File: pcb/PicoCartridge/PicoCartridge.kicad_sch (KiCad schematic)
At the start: 0 parts

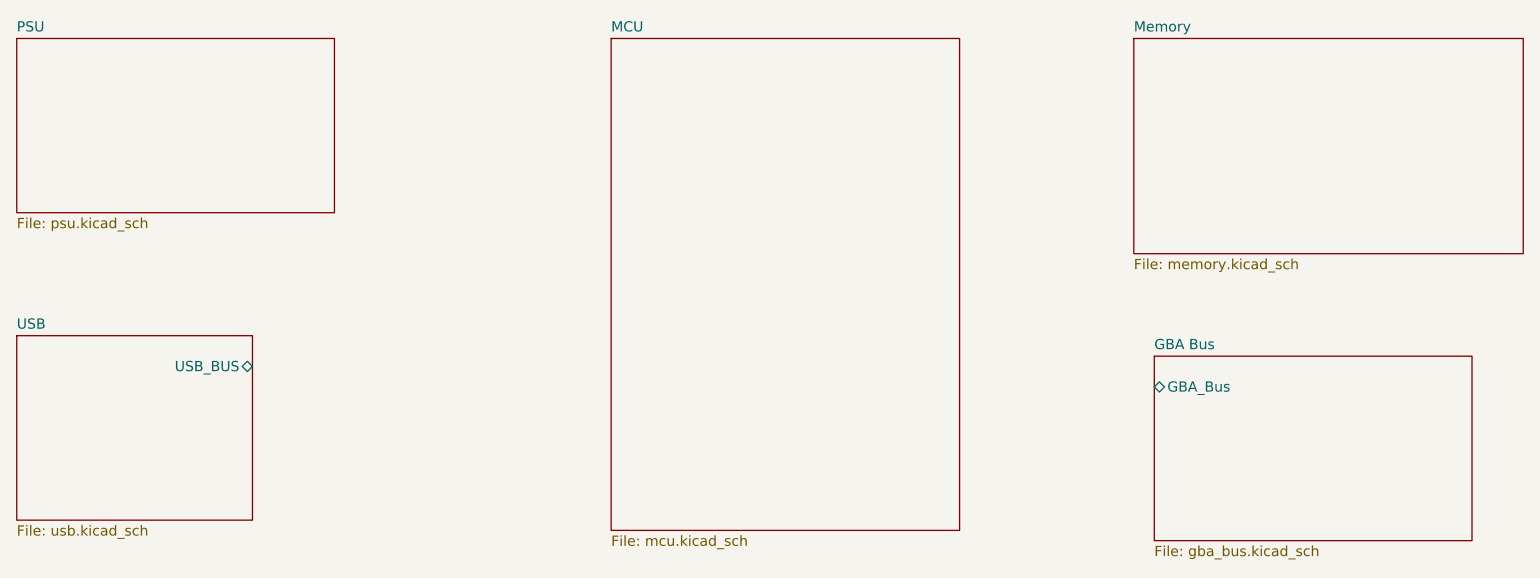
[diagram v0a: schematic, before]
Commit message: Defined additional interfaces
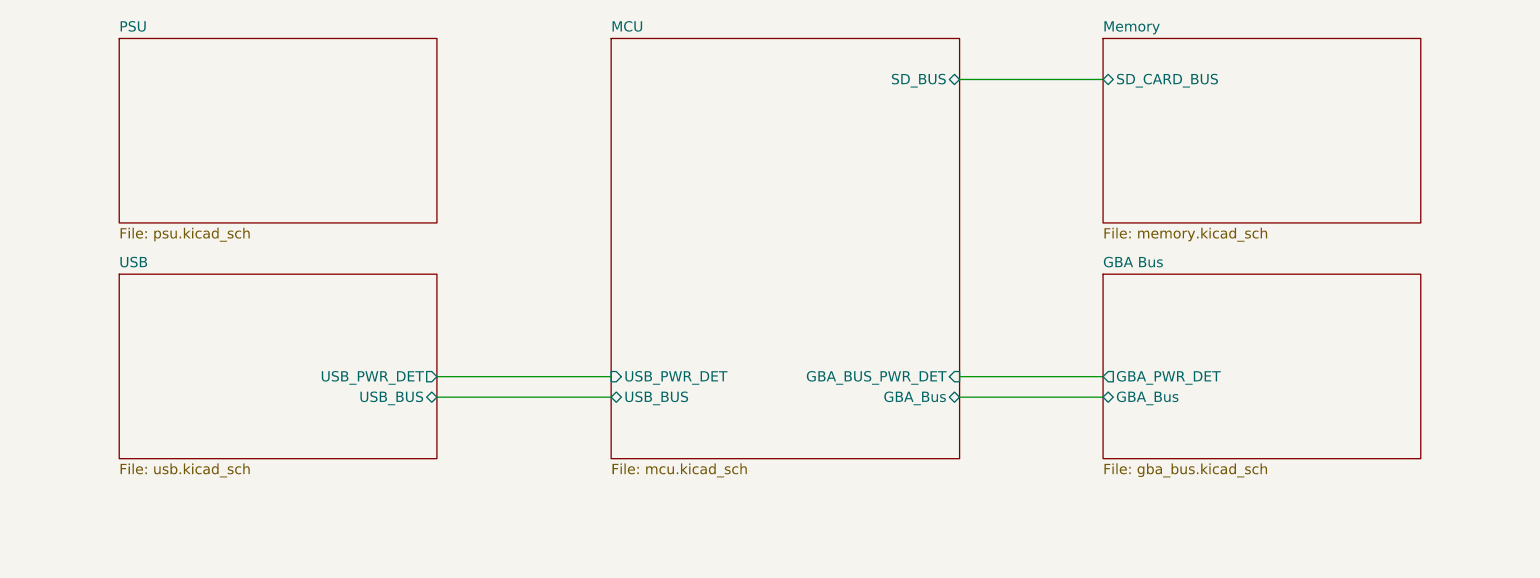
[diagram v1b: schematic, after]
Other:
- sheet GBA Bus ports: added GBA_PWR_DET; removed none
- sheet MCU ports: added GBA_BUS_PWR_DET, GBA_Bus, SD_BUS, USB_BUS, USB_PWR_DET; removed none
- sheet Memory ports: added SD_CARD_BUS; removed none
- sheet USB ports: added USB_PWR_DET; removed none
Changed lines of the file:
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@@
 	(generator_version "8.0")
 	(paper "A4")
-	(sheet
-		(at 21.59 25.4)
-		(size 39.37 21.59)
+	(wire
+		(pts
+			(xy 138.43 30.48) (xy 156.21 30.48)
+		)
+		(stroke
+			(width 0)
+			(type default)
+		)
+	)
+	(wire
+		(pts
+			(xy 138.43 69.85) (xy 156.21 69.85)
+		)
+		(stroke
+			(width 0)
+			(type default)
+		)
+	)
+	(wire
+		(pts
+			(xy 73.66 69.85) (xy 95.25 69.85)
+		)
+		(stroke
+			(width 0)
+			(type default)
+		)
+	)
+	(wire
+		(pts
+			(xy 73.66 67.31) (xy 95.25 67.31)
+		)
+		(stroke
+			(width 0)
+			(type default)
+		)
+	)
+	(wire
+		(pts
+			(xy 138.43 67.31) (xy 156.21 67.31)
+		)
+		(stroke
+			(width 0)
+			(type default)
+		)
+	)
+	(sheet
+		(at 34.29 25.4)
+		(size 39.37 22.86)
 		(fields_autoplaced yes)
 		(stroke
@@
 		)
 		(property "Sheetname" "PSU"
-			(at 21.59 24.6884 0)
+			(at 34.29 24.6884 0)
 			(effects
 				(font
@@
 		)
 		(property "Sheetfile" "psu.kicad_sch"
-			(at 21.59 47.5746 0)
+			(at 34.29 48.8446 0)
 			(effects
 				(font
@@
 	)
 	(sheet
-		(at 162.56 64.77)
+		(at 156.21 54.61)
 		(size 39.37 22.86)
 		(fields_autoplaced yes)
@@
 		)
 		(property "Sheetname" "GBA Bus"
-			(at 162.56 64.0584 0)
+			(at 156.21 53.8984 0)
 			(effects
 				(font
@@
 		)
 		(property "Sheetfile" "gba_bus.kicad_sch"
-			(at 162.56 88.2146 0)
+			(at 156.21 78.0546 0)
 			(effects
 				(font
@@
 		)
 		(pin "GBA_Bus" bidirectional
-			(at 162.56 68.58 180)
+			(at 156.21 69.85 180)
+			(effects
+				(font
+					(size 1.27 1.27)
+				)
+				(justify left)
+			)
+		)
+		(pin "GBA_PWR_DET" output
+			(at 156.21 67.31 180)
 			(effects
 				(font
@@
 	)
 	(sheet
-		(at 21.59 62.23)
-		(size 29.21 22.86)
+		(at 34.29 54.61)
+		(size 39.37 22.86)
 		(fields_autoplaced yes)
 		(stroke
@@
 		)
 		(property "Sheetname" "USB"
-			(at 21.59 61.5184 0)
+			(at 34.29 53.8984 0)
 			(effects
 				(font
@@
 		)
 		(property "Sheetfile" "usb.kicad_sch"
-			(at 21.59 85.6746 0)
+			(at 34.29 78.0546 0)
 			(effects
 				(font
@@
 		)
 		(pin "USB_BUS" bidirectional
-			(at 50.8 66.04 0)
+			(at 73.66 69.85 0)
+			(effects
+				(font
+					(size 1.27 1.27)
+				)
+				(justify right)
+			)
+		)
+		(pin "USB_PWR_DET" output
+			(at 73.66 67.31 0)
 			(effects
 				(font
@@
 	)
 	(sheet
-		(at 160.02 25.4)
-		(size 48.26 26.67)
+		(at 156.21 25.4)
+		(size 39.37 22.86)
 		(fields_autoplaced yes)
 		(stroke
@@
 		)
 		(property "Sheetname" "Memory"
-			(at 160.02 24.6884 0)
+			(at 156.21 24.6884 0)
 			(effects
 				(font
@@
 		)
 		(property "Sheetfile" "memory.kicad_sch"
-			(at 160.02 52.6546 0)
-			(effects
-				(font
-					(size 1.27 1.27)
-				)
-				(justify left top)
+			(at 156.21 48.8446 0)
+			(effects
+				(font
+					(size 1.27 1.27)
+				)
+				(justify left top)
+			)
+		)
+		(pin "SD_CARD_BUS" bidirectional
+			(at 156.21 30.48 180)
+			(effects
+				(font
+					(size 1.27 1.27)
+				)
+				(justify left)
 			)
 		)
@@
 	(sheet
 		(at 95.25 25.4)
-		(size 43.18 60.96)
+		(size 43.18 52.07)
 		(fields_autoplaced yes)
 		(stroke
@@
 		)
 		(property "Sheetfile" "mcu.kicad_sch"
-			(at 95.25 86.9446 0)
-			(effects
-				(font
-					(size 1.27 1.27)
-				)
-				(justify left top)
-			)
-		)
+			(at 95.25 78.0546 0)
+			(effects
+				(font
+					(size 1.27 1.27)
+				)
+				(justify left top)
+			)
+		)
+		(pin "USB_PWR_DET" input
+			(at 95.25 67.31 180)
+			(effects
+				(font
+					(size 1.27 1.27)
+				)
+				(justify left)
+			)
+		)
+		(pin "GBA_BUS_PWR_DET" input
+			(at 138.43 67.31 0)
+			(effects
+				(font
+					(size 1.27 1.27)
+				)
+				(justify right)
+			)
+		)
+		(pin "SD_BUS" bidirectional
+			(at 138.43 30.48 0)
+			(effects
+				(font
+					(size 1.27 1.27)
+				)
+				(justify right)
+			)
+		)
+		(pin "GBA_Bus" bidirectional
+			(at 138.43 69.85 0)
+			(effects
+				(font
+					(size 1.27 1.27)
+				)
+				(justify right)
+			)
+		)
+		(pin "USB_BUS" bidirectional
+			(at 95.25 69.85 180)
+			(effects
+				(font
+					(size 1.27 1.27)
+				)
+				(justify left)
+			)
+		)

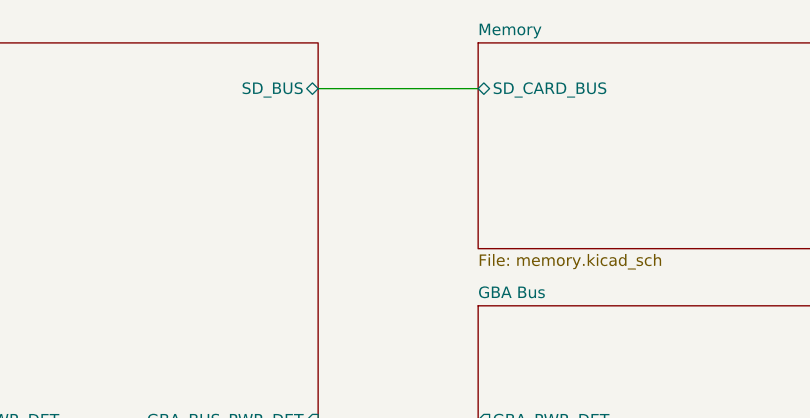
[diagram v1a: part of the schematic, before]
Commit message: Fixed connection between MCU and SD card
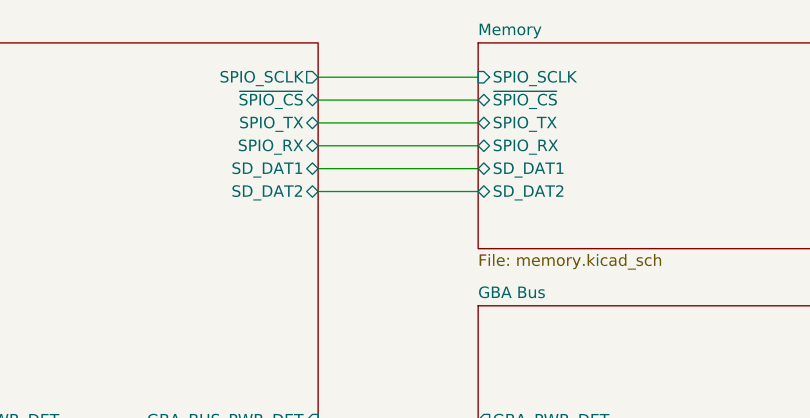
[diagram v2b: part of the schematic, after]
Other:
- sheet MCU ports: added SD_DAT1, SD_DAT2, SPIO_RX, SPIO_SCLK, SPIO_TX, ~{SPIO_CS}; removed SD_BUS
- sheet Memory ports: added SD_DAT1, SD_DAT2, SPIO_RX, SPIO_SCLK, SPIO_TX, ~{SPIO_CS}; removed SD_CARD_BUS
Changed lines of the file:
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@@
 	(wire
 		(pts
-			(xy 138.43 30.48) (xy 156.21 30.48)
+			(xy 138.43 31.75) (xy 156.21 31.75)
+		)
+		(stroke
+			(width 0)
+			(type default)
+		)
+	)
+	(wire
+		(pts
+			(xy 138.43 36.83) (xy 156.21 36.83)
+		)
+		(stroke
+			(width 0)
+			(type default)
+		)
+	)
+	(wire
+		(pts
+			(xy 138.43 29.21) (xy 156.21 29.21)
+		)
+		(stroke
+			(width 0)
+			(type default)
+		)
+	)
+	(wire
+		(pts
+			(xy 138.43 41.91) (xy 156.21 41.91)
 		)
 		(stroke
@@
 	(wire
 		(pts
+			(xy 138.43 39.37) (xy 156.21 39.37)
+		)
+		(stroke
+			(width 0)
+			(type default)
+		)
+	)
+	(wire
+		(pts
 			(xy 73.66 69.85) (xy 95.25 69.85)
+		)
+		(stroke
+			(width 0)
+			(type default)
+		)
+	)
+	(wire
+		(pts
+			(xy 138.43 34.29) (xy 156.21 34.29)
 		)
 		(stroke
@@
 			)
 		)
-		(pin "SD_CARD_BUS" bidirectional
-			(at 156.21 30.48 180)
+		(pin "~{SPIO_CS}" bidirectional
+			(at 156.21 31.75 180)
+			(effects
+				(font
+					(size 1.27 1.27)
+				)
+				(justify left)
+			)
+		)
+		(pin "SPIO_TX" bidirectional
+			(at 156.21 34.29 180)
+			(effects
+				(font
+					(size 1.27 1.27)
+				)
+				(justify left)
+			)
+		)
+		(pin "SD_DAT2" bidirectional
+			(at 156.21 41.91 180)
+			(effects
+				(font
+					(size 1.27 1.27)
+				)
+				(justify left)
+			)
+		)
+		(pin "SPIO_RX" bidirectional
+			(at 156.21 36.83 180)
+			(effects
+				(font
+					(size 1.27 1.27)
+				)
+				(justify left)
+			)
+		)
+		(pin "SD_DAT1" bidirectional
+			(at 156.21 39.37 180)
+			(effects
+				(font
+					(size 1.27 1.27)
+				)
+				(justify left)
+			)
+		)
+		(pin "SPIO_SCLK" input
+			(at 156.21 29.21 180)
 			(effects
 				(font
@@
 			)
 		)
-		(pin "SD_BUS" bidirectional
-			(at 138.43 30.48 0)
-			(effects
-				(font
-					(size 1.27 1.27)
-				)
-				(justify right)
-			)
-		)
 		(pin "GBA_Bus" bidirectional
 			(at 138.43 69.85 0)
@@
 			)
 		)
+		(pin "SPIO_SCLK" output
+			(at 138.43 29.21 0)
+			(effects
+				(font
+					(size 1.27 1.27)
+				)
+				(justify right)
+			)
+		)
+		(pin "SPIO_TX" bidirectional
+			(at 138.43 34.29 0)
+			(effects
+				(font
+					(size 1.27 1.27)
+				)
+				(justify right)
+			)
+		)
+		(pin "~{SPIO_CS}" bidirectional
+			(at 138.43 31.75 0)
+			(effects
+				(font
+					(size 1.27 1.27)
+				)
+				(justify right)
+			)
+		)
+		(pin "SPIO_RX" bidirectional
+			(at 138.43 36.83 0)
+			(effects
+				(font
+					(size 1.27 1.27)
+				)
+				(justify right)
+			)
+		)
+		(pin "SD_DAT2" bidirectional
+			(at 138.43 41.91 0)
+			(effects
+				(font
+					(size 1.27 1.27)
+				)
+				(justify right)
+			)
+		)
+		(pin "SD_DAT1" bidirectional
+			(at 138.43 39.37 0)
+			(effects
+				(font
+					(size 1.27 1.27)
+				)
+				(justify right)
+			)
+		)

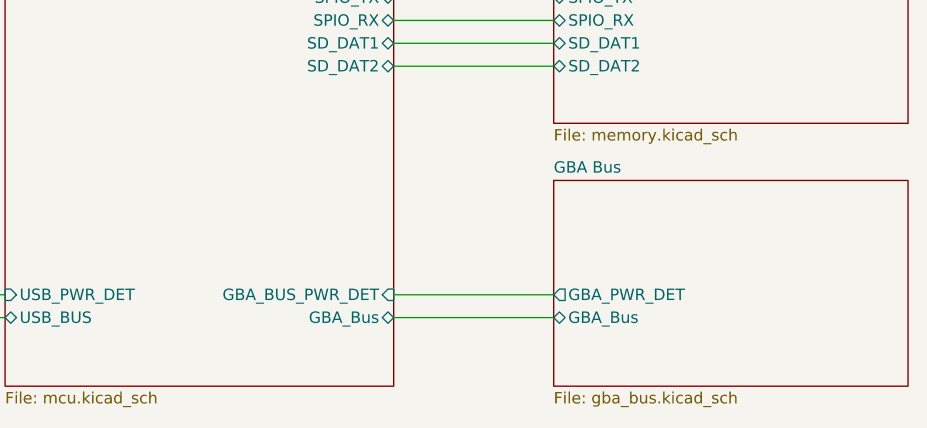
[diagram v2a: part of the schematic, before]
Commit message: Fixed GBA bus internal logic
THe GBA bus is now a correct bus in a sense of kicad
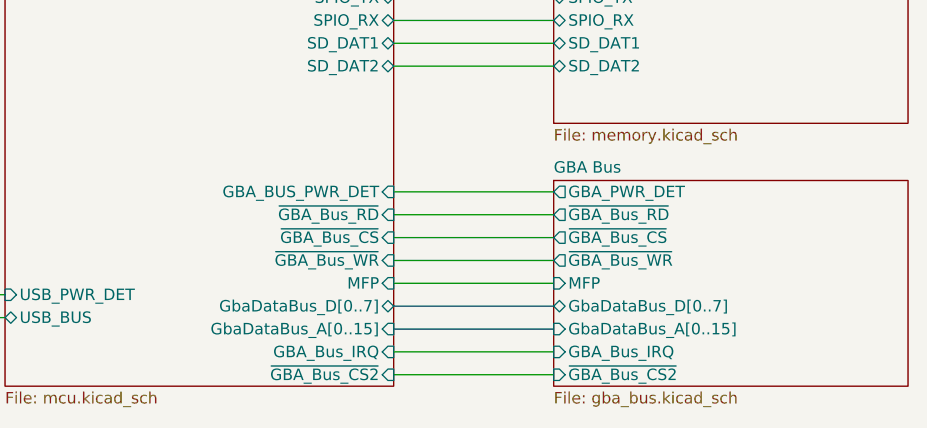
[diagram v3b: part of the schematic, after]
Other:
- sheet GBA Bus ports: added GBA_Bus_IRQ, GbaDataBus_A[0..15], GbaDataBus_D[0..7], MFP, ~{GBA_Bus_CS2}, ~{GBA_Bus_CS}, ~{GBA_Bus_RD}, ~{GBA_Bus_WR}; removed GBA_Bus
- sheet MCU ports: added GBA_Bus_IRQ, GbaDataBus_A[0..15], GbaDataBus_D[0..7], MFP, ~{GBA_Bus_CS2}, ~{GBA_Bus_CS}, ~{GBA_Bus_RD}, ~{GBA_Bus_WR}; removed GBA_Bus
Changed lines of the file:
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@@
+	(wire
+		(pts
+			(xy 138.43 73.66) (xy 156.21 73.66)
+		)
+		(stroke
+			(width 0)
+			(type default)
+		)
+	)
 	(wire
 		(pts
@@
 	(wire
 		(pts
-			(xy 138.43 69.85) (xy 156.21 69.85)
+			(xy 138.43 55.88) (xy 156.21 55.88)
 		)
 		(stroke
@@
 	(wire
 		(pts
+			(xy 138.43 63.5) (xy 156.21 63.5)
+		)
+		(stroke
+			(width 0)
+			(type default)
+		)
+	)
+	(wire
+		(pts
 			(xy 73.66 69.85) (xy 95.25 69.85)
 		)
@@
 		)
 	)
+	(bus
+		(pts
+			(xy 138.43 71.12) (xy 156.21 71.12)
+		)
+		(stroke
+			(width 0)
+			(type default)
+		)
+	)
 	(wire
 		(pts
@@
 	(wire
 		(pts
+			(xy 138.43 58.42) (xy 156.21 58.42)
+		)
+		(stroke
+			(width 0)
+			(type default)
+		)
+	)
+	(wire
+		(pts
+			(xy 138.43 60.96) (xy 156.21 60.96)
+		)
+		(stroke
+			(width 0)
+			(type default)
+		)
+	)
+	(wire
+		(pts
+			(xy 138.43 66.04) (xy 156.21 66.04)
+		)
+		(stroke
+			(width 0)
+			(type default)
+		)
+	)
+	(wire
+		(pts
 			(xy 73.66 67.31) (xy 95.25 67.31)
 		)
@@
 	(wire
 		(pts
-			(xy 138.43 67.31) (xy 156.21 67.31)
+			(xy 138.43 76.2) (xy 156.21 76.2)
+		)
+		(stroke
+			(width 0)
+			(type default)
+		)
+	)
+	(bus
+		(pts
+			(xy 138.43 68.58) (xy 156.21 68.58)
 		)
 		(stroke
@@
 			)
 		)
-		(pin "GBA_Bus" bidirectional
-			(at 156.21 69.85 180)
+		(pin "MFP" input
+			(at 156.21 66.04 180)
+			(effects
+				(font
+					(size 1.27 1.27)
+				)
+				(justify left)
+			)
+		)
+		(pin "~{GBA_Bus_RD}" output
+			(at 156.21 58.42 180)
+			(effects
+				(font
+					(size 1.27 1.27)
+				)
+				(justify left)
+			)
+		)
+		(pin "~{GBA_Bus_WR}" output
+			(at 156.21 63.5 180)
+			(effects
+				(font
+					(size 1.27 1.27)
+				)
+				(justify left)
+			)
+		)
+		(pin "~{GBA_Bus_CS}" output
+			(at 156.21 60.96 180)
+			(effects
+				(font
+					(size 1.27 1.27)
+				)
+				(justify left)
+			)
+		)
+		(pin "GbaDataBus_D[0..7]" bidirectional
+			(at 156.21 68.58 180)
+			(effects
+				(font
+					(size 1.27 1.27)
+				)
+				(justify left)
+			)
+		)
+		(pin "GbaDataBus_A[0..15]" input
+			(at 156.21 71.12 180)
+			(effects
+				(font
+					(size 1.27 1.27)
+				)
+				(justify left)
+			)
+		)
+		(pin "GBA_Bus_IRQ" input
+			(at 156.21 73.66 180)
+			(effects
+				(font
+					(size 1.27 1.27)
+				)
+				(justify left)
+			)
+		)
+		(pin "~{GBA_Bus_CS2}" input
+			(at 156.21 76.2 180)
 			(effects
 				(font
@@
 		)
 		(pin "GBA_PWR_DET" output
-			(at 156.21 67.31 180)
+			(at 156.21 55.88 180)
 			(effects
 				(font
@@
 			)
 		)
-		(pin "GBA_BUS_PWR_DET" input
-			(at 138.43 67.31 0)
-			(effects
-				(font
-					(size 1.27 1.27)
-				)
-				(justify right)
-			)
-		)
-		(pin "GBA_Bus" bidirectional
-			(at 138.43 69.85 0)
-			(effects
-				(font
-					(size 1.27 1.27)
-				)
-				(justify right)
-			)
-		)
 		(pin "USB_BUS" bidirectional
 			(at 95.25 69.85 180)
@@
 			(effects
 				(font
+					(size 1.27 1.27)
+				)
+				(justify right)
+			)
+		)
+		(pin "~{GBA_Bus_CS2}" input
+			(at 138.43 76.2 0)
+			(effects
+				(font
+					(size 1.27 1.27)
+				)
+				(justify right)
+			)
+		)
+		(pin "GBA_Bus_IRQ" input
+			(at 138.43 73.66 0)
+			(effects
+				(font
+					(size 1.27 1.27)
+				)
+				(justify right)
+			)
+		)
+		(pin "GBA_BUS_PWR_DET" input
+			(at 138.43 55.88 0)
+			(effects
+				(font
+					(size 1.27 1.27)
+				)
+				(justify right)
+			)
+		)
+		(pin "~{GBA_Bus_RD}" input
+			(at 138.43 58.42 0)
+			(effects
+				(font
+					(size 1.27 1.27)
+				)
+				(justify right)
+			)
+		)
+		(pin "~{GBA_Bus_CS}" input
+			(at 138.43 60.96 0)
+			(effects
+				(font
+					(size 1.27 1.27)
+				)
+				(justify right)
+			)
+		)
+		(pin "~{GBA_Bus_WR}" input
+			(at 138.43 63.5 0)
+			(effects
+				(font
+					(size 1.27 1.27)
+				)
+				(justify right)
+			)
+		)
+		(pin "MFP" input
+			(at 138.43 66.04 0)
+			(effects
+				(font
+					(size 1.27 1.27)
+				)
+				(justify right)
+			)
+		)
+		(pin "GbaDataBus_D[0..7]" bidirectional
+			(at 138.43 68.58 0)
+			(effects
+				(font
+					(size 1.27 1.27)
+				)
+				(justify right)
+			)
+		)
+		(pin "GbaDataBus_A[0..15]" input
+			(at 138.43 71.12 0)
+			(effects
+				(font
